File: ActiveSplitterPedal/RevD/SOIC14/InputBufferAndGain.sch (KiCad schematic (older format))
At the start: 7 parts, among them U2 TL072

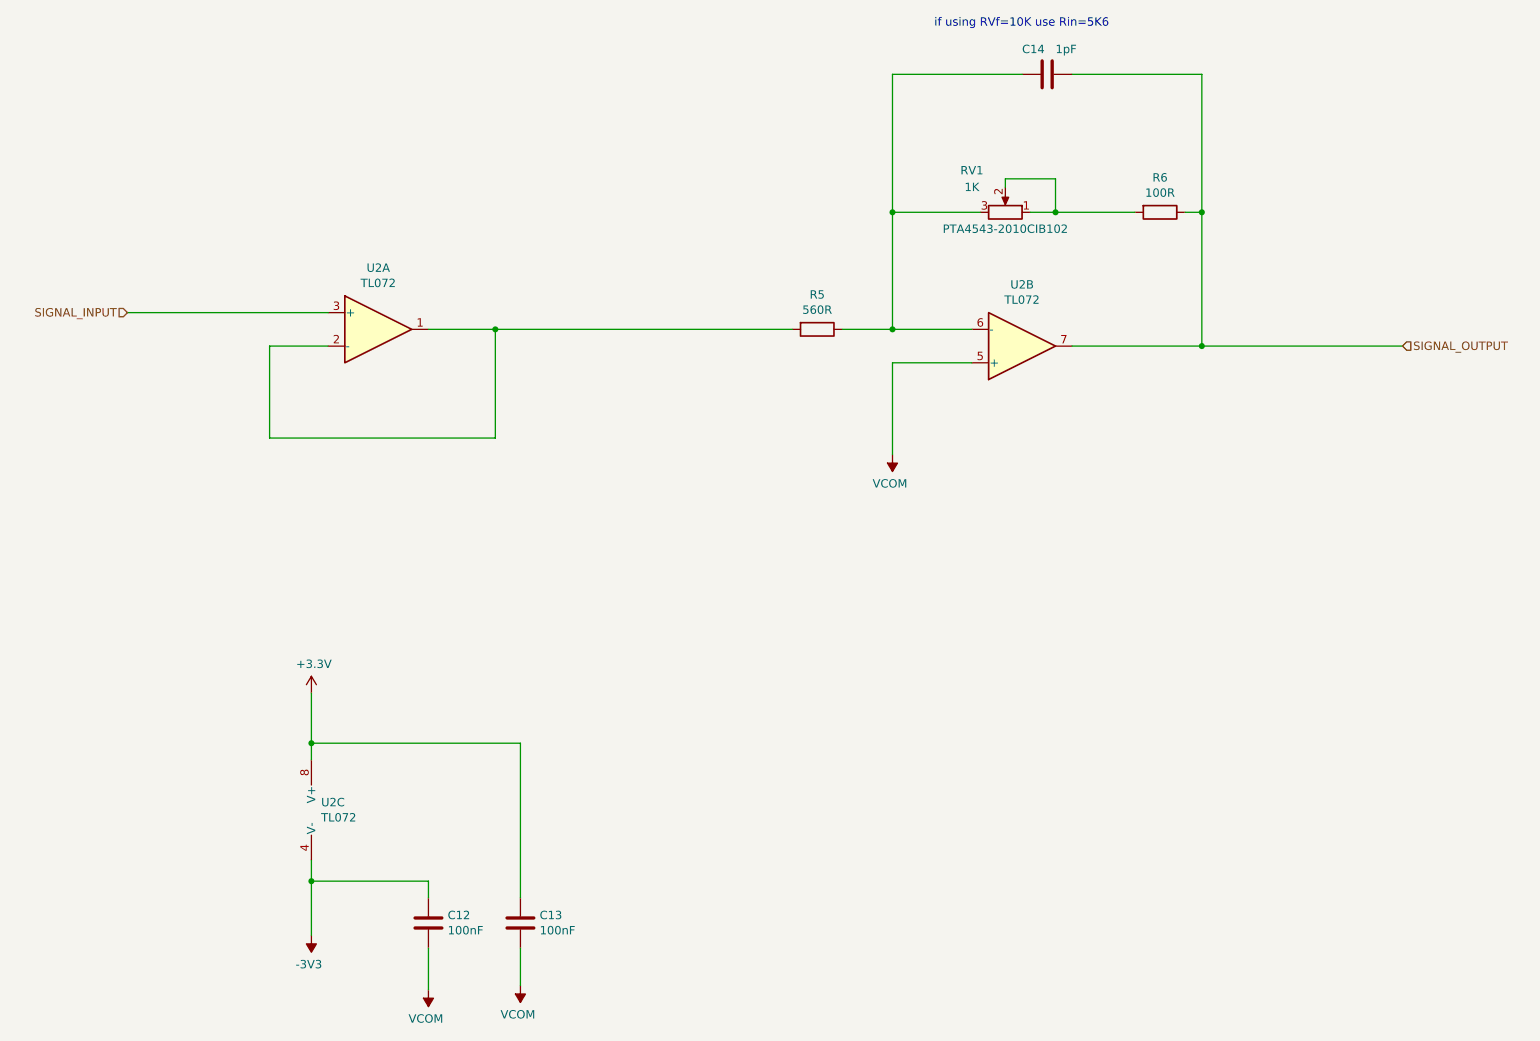
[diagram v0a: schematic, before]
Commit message: fixed peak detector
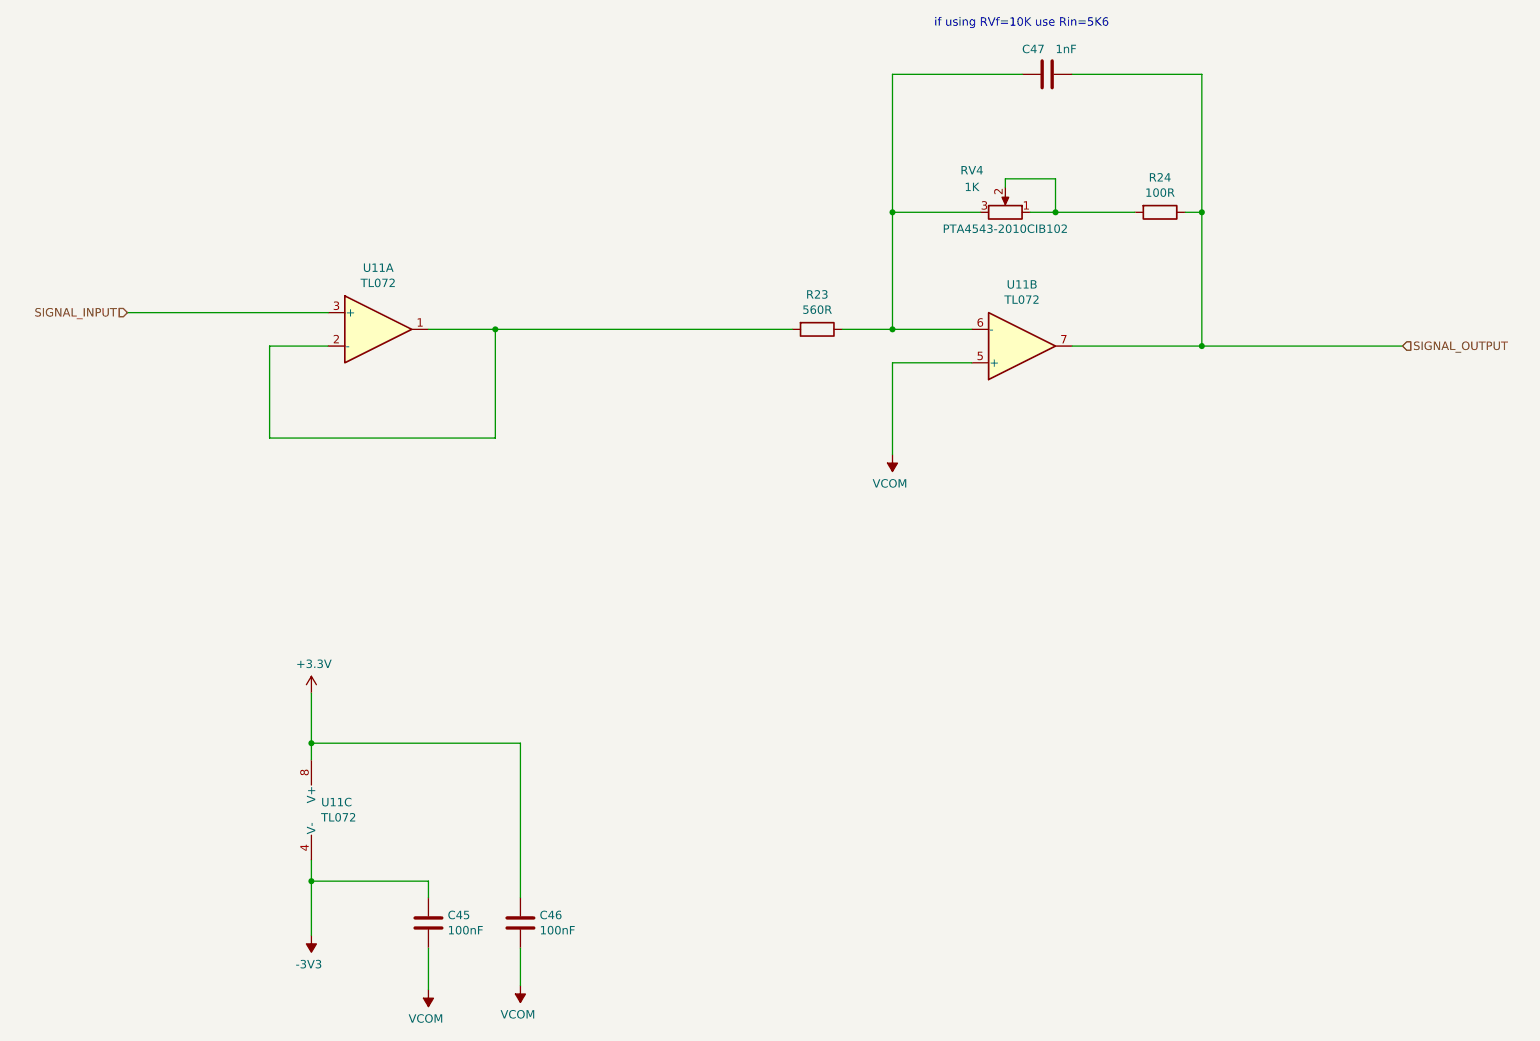
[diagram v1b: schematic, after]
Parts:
- C14: value 1pF -> 1nF
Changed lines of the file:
@@
 AR Path="/5F6A445C/5F59292E" Ref="R17"  Part="1"
 AR Path="/5F6AEF24/5F59292E" Ref="R23"  Part="1"
-F 0 "R5" V 6018 2875 50  0000 C CNN
+F 0 "R23" V 6018 2875 50  0000 C CNN
 F 1 "560R" V 6109 2875 50  0000 C CNN
 F 2 "Resistor_SMD:R_0805_2012Metric_Pad1.15x1.40mm_HandSolder" V 6155 2875 50  0001 C CNN
@@
 AR Path="/5F6A445C/5F59293F" Ref="RV3"  Part="1"
 AR Path="/5F6AEF24/5F59293F" Ref="RV4"  Part="1"
-F 0 "RV1" V 7600 1975 50  0000 C CNN
+F 0 "RV4" V 7600 1975 50  0000 C CNN
 F 1 "1K" V 7500 1975 50  0000 C CNN
 F 2 "Bourn_PTA_Slider:Slider_PTA4543_60MM" H 7350 2175 50  0001 C CNN
@@
 AR Path="/5F6A445C/5F592956" Ref="R18"  Part="1"
 AR Path="/5F6AEF24/5F592956" Ref="R24"  Part="1"
-F 0 "R6" V 8068 2175 50  0000 C CNN
+F 0 "R24" V 8068 2175 50  0000 C CNN
 F 1 "100R" V 8159 2175 50  0000 C CNN
 F 2 "Resistor_SMD:R_0805_2012Metric_Pad1.15x1.40mm_HandSolder" V 8205 2175 50  0001 C CNN
@@
 AR Path="/5F6A445C/5F59295D" Ref="C36"  Part="1"
 AR Path="/5F6AEF24/5F59295D" Ref="C47"  Part="1"
-F 0 "C14" V 7450 1200 50  0000 L CNN
-F 1 "1pF" V 7450 1400 50  0000 L CNN
+F 0 "C47" V 7450 1200 50  0000 L CNN
+F 1 "1nF" V 7450 1400 50  0000 L CNN
 F 2 "Capacitor_SMD:C_0805_2012Metric_Pad1.15x1.40mm_HandSolder" H 7638 1200 50  0001 C CNN
 F 3 "~" H 7600 1350 50  0001 C CNN
@@
 AR Path="/5F6A445C/5F59AE7C" Ref="U8"  Part="1"
 AR Path="/5F6AEF24/5F59AE7C" Ref="U11"  Part="1"
-F 0 "U2" H 3600 3242 50  0000 C CNN
+F 0 "U11" H 3600 3242 50  0000 C CNN
 F 1 "TL072" H 3600 3151 50  0000 C CNN
 F 2 "Package_SO:SOIC-8_3.9x4.9mm_P1.27mm" H 3600 2875 50  0001 C CNN
@@
 AR Path="/5F6A445C/5F59C9C2" Ref="U8"  Part="2"
 AR Path="/5F6AEF24/5F59C9C2" Ref="U11"  Part="2"
-F 0 "U2" H 7450 2608 50  0000 C CNN
+F 0 "U11" H 7450 2608 50  0000 C CNN
 F 1 "TL072" H 7450 2699 50  0000 C CNN
 F 2 "Package_SO:SOIC-8_3.9x4.9mm_P1.27mm" H 7450 2975 50  0001 C CNN
@@
 AR Path="/5F6A445C/5F59E5A5" Ref="U8"  Part="3"
 AR Path="/5F6AEF24/5F59E5A5" Ref="U11"  Part="3"
-F 0 "U2" H 3258 5796 50  0000 L CNN
+F 0 "U11" H 3258 5796 50  0000 L CNN
 F 1 "TL072" H 3258 5705 50  0000 L CNN
 F 2 "Package_SO:SOIC-8_3.9x4.9mm_P1.27mm" H 3300 5750 50  0001 C CNN
@@
 AR Path="/5F6A445C/5F5D3555" Ref="C34"  Part="1"
 AR Path="/5F6AEF24/5F5D3555" Ref="C45"  Part="1"
-F 0 "C12" H 4015 6471 50  0000 L CNN
+F 0 "C45" H 4015 6471 50  0000 L CNN
 F 1 "100nF" H 4015 6380 50  0000 L CNN
 F 2 "Capacitor_SMD:C_0805_2012Metric_Pad1.15x1.40mm_HandSolder" H 3938 6275 50  0001 C CNN
@@
 AR Path="/5F6A445C/5F5D446F" Ref="C35"  Part="1"
 AR Path="/5F6AEF24/5F5D446F" Ref="C46"  Part="1"
-F 0 "C13" H 4565 6471 50  0000 L CNN
+F 0 "C46" H 4565 6471 50  0000 L CNN
 F 1 "100nF" H 4565 6380 50  0000 L CNN
 F 2 "Capacitor_SMD:C_0805_2012Metric_Pad1.15x1.40mm_HandSolder" H 4488 6275 50  0001 C CNN
@@
 AR Path="/5F6A445C/5F594A1A" Ref="#PWR0135"  Part="1"
 AR Path="/5F6AEF24/5F594A1A" Ref="#PWR0147"  Part="1"
-F 0 "#PWR0111" H 3900 6675 50  0001 C CNN
+F 0 "#PWR0147" H 3900 6675 50  0001 C CNN
 F 1 "VCOM" H 3915 6998 50  0000 C CNN
 F 2 "" H 3900 6825 50  0001 C CNN
@@
 AR Path="/5F6A445C/5F59500E" Ref="#PWR0136"  Part="1"
 AR Path="/5F6AEF24/5F59500E" Ref="#PWR0148"  Part="1"
-F 0 "#PWR0112" H 4450 6650 50  0001 C CNN
+F 0 "#PWR0148" H 4450 6650 50  0001 C CNN
 F 1 "VCOM" H 4465 6973 50  0000 C CNN
 F 2 "" H 4450 6800 50  0001 C CNN
@@
 AR Path="/5F6A445C/5F595416" Ref="#PWR0137"  Part="1"
 AR Path="/5F6AEF24/5F595416" Ref="#PWR0149"  Part="1"
-F 0 "#PWR0113" H 6675 3475 50  0001 C CNN
+F 0 "#PWR0149" H 6675 3475 50  0001 C CNN
 F 1 "VCOM" H 6690 3798 50  0000 C CNN
 F 2 "" H 6675 3625 50  0001 C CNN
@@
 AR Path="/5F6A445C/5F595ABA" Ref="#PWR0138"  Part="1"
 AR Path="/5F6AEF24/5F595ABA" Ref="#PWR0150"  Part="1"
-F 0 "#PWR0114" H 3200 6600 50  0001 C CNN
+F 0 "#PWR0150" H 3200 6600 50  0001 C CNN
 F 1 "-3V3" H 3215 6673 50  0000 C CNN
 F 2 "" H 3200 6500 50  0001 C CNN
@@
 AR Path="/5F6A445C/5F596316" Ref="#PWR0139"  Part="1"
 AR Path="/5F6AEF24/5F596316" Ref="#PWR0151"  Part="1"
-F 0 "#PWR0115" H 3200 4900 50  0001 C CNN
+F 0 "#PWR0151" H 3200 4900 50  0001 C CNN
 F 1 "+3.3V" H 3215 5223 50  0000 C CNN
 F 2 "" H 3200 5050 50  0001 C CNN

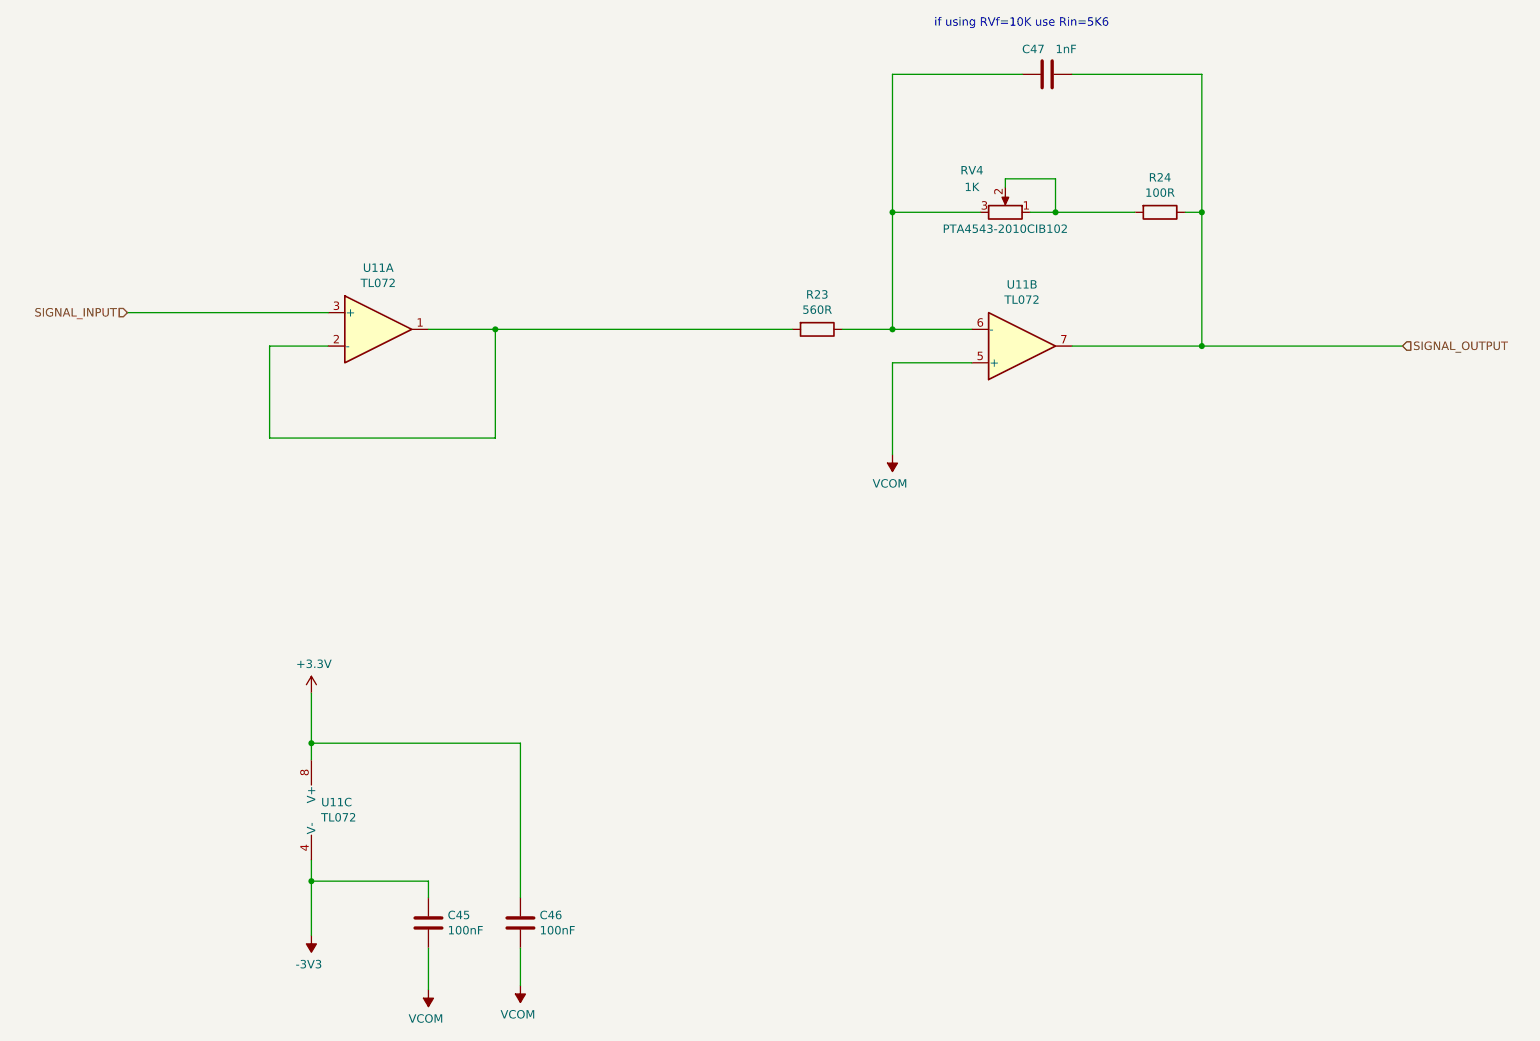
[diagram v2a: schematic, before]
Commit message: updated hw
- Changed peak detector gain feedback resistor to 10K
- Changed peak detector storage cap to 100nF
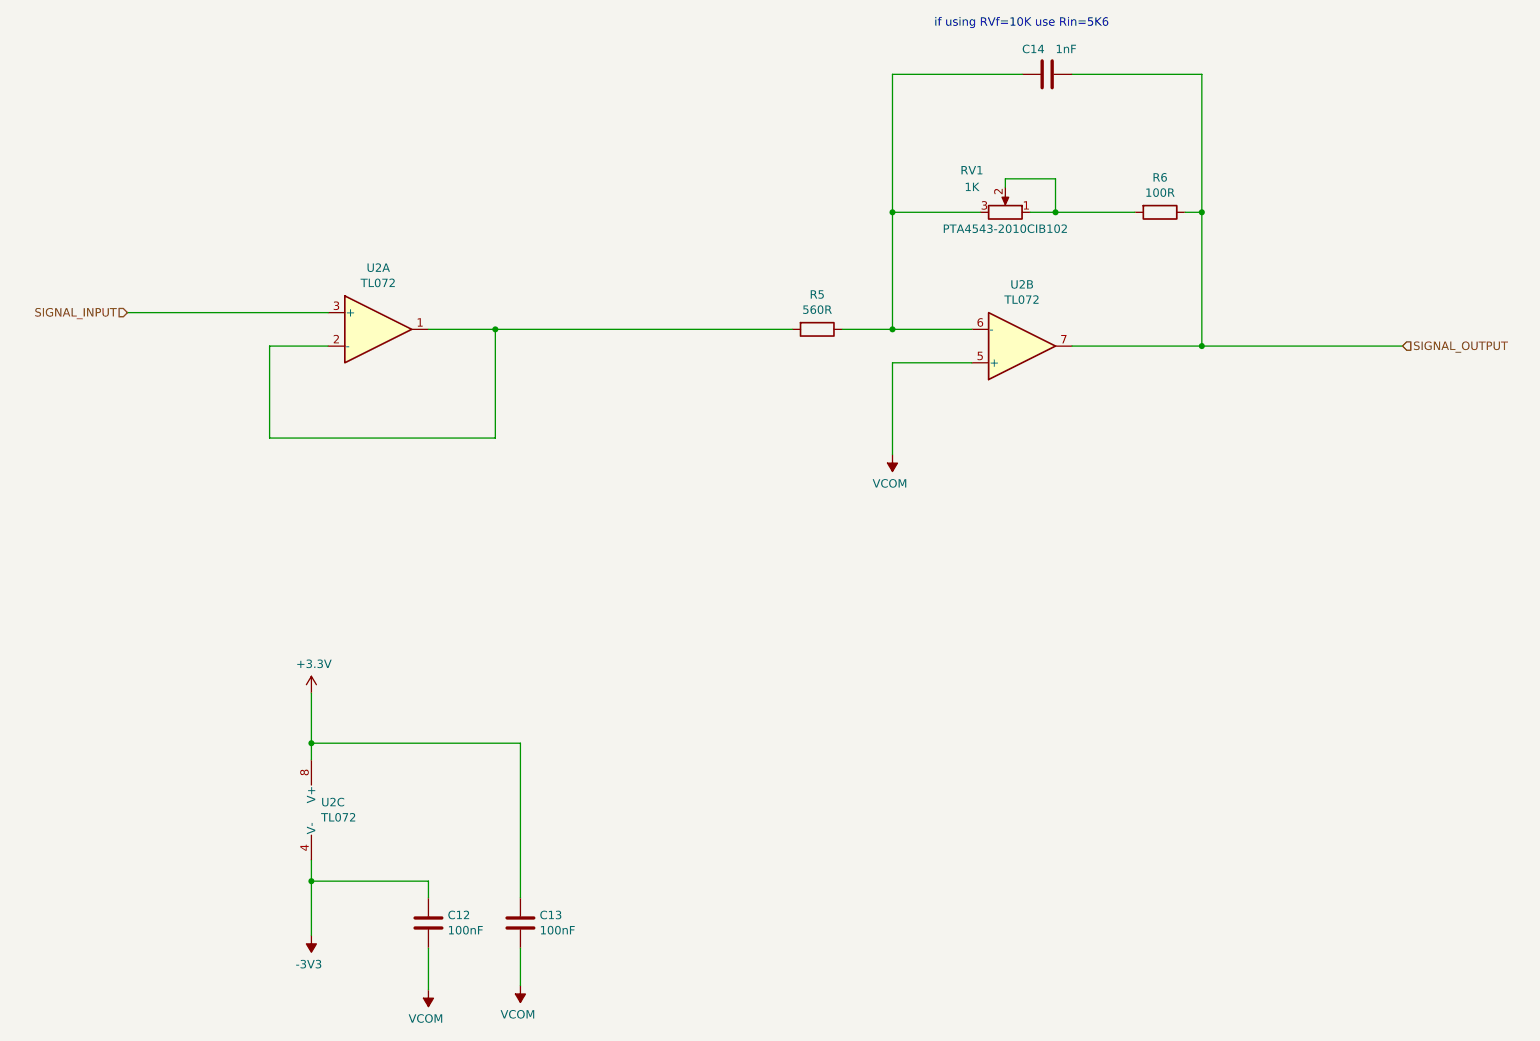
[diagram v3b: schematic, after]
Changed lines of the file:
@@
 $Descr A4 11693 8268
 encoding utf-8
-Sheet 10 10
+Sheet 4 10
 Title ""
 Date ""
@@
 AR Path="/5F6A445C/5F59292E" Ref="R17"  Part="1"
 AR Path="/5F6AEF24/5F59292E" Ref="R23"  Part="1"
-F 0 "R23" V 6018 2875 50  0000 C CNN
+F 0 "R5" V 6018 2875 50  0000 C CNN
 F 1 "560R" V 6109 2875 50  0000 C CNN
 F 2 "Resistor_SMD:R_0805_2012Metric_Pad1.15x1.40mm_HandSolder" V 6155 2875 50  0001 C CNN
@@
 AR Path="/5F6A445C/5F59293F" Ref="RV3"  Part="1"
 AR Path="/5F6AEF24/5F59293F" Ref="RV4"  Part="1"
-F 0 "RV4" V 7600 1975 50  0000 C CNN
+F 0 "RV1" V 7600 1975 50  0000 C CNN
 F 1 "1K" V 7500 1975 50  0000 C CNN
 F 2 "Bourn_PTA_Slider:Slider_PTA4543_60MM" H 7350 2175 50  0001 C CNN
@@
 AR Path="/5F6A445C/5F592956" Ref="R18"  Part="1"
 AR Path="/5F6AEF24/5F592956" Ref="R24"  Part="1"
-F 0 "R24" V 8068 2175 50  0000 C CNN
+F 0 "R6" V 8068 2175 50  0000 C CNN
 F 1 "100R" V 8159 2175 50  0000 C CNN
 F 2 "Resistor_SMD:R_0805_2012Metric_Pad1.15x1.40mm_HandSolder" V 8205 2175 50  0001 C CNN
@@
 AR Path="/5F6A445C/5F59295D" Ref="C36"  Part="1"
 AR Path="/5F6AEF24/5F59295D" Ref="C47"  Part="1"
-F 0 "C47" V 7450 1200 50  0000 L CNN
+F 0 "C14" V 7450 1200 50  0000 L CNN
 F 1 "1nF" V 7450 1400 50  0000 L CNN
 F 2 "Capacitor_SMD:C_0805_2012Metric_Pad1.15x1.40mm_HandSolder" H 7638 1200 50  0001 C CNN
@@
 AR Path="/5F6A445C/5F59AE7C" Ref="U8"  Part="1"
 AR Path="/5F6AEF24/5F59AE7C" Ref="U11"  Part="1"
-F 0 "U11" H 3600 3242 50  0000 C CNN
+F 0 "U2" H 3600 3242 50  0000 C CNN
 F 1 "TL072" H 3600 3151 50  0000 C CNN
 F 2 "Package_SO:SOIC-8_3.9x4.9mm_P1.27mm" H 3600 2875 50  0001 C CNN
@@
 AR Path="/5F6A445C/5F59C9C2" Ref="U8"  Part="2"
 AR Path="/5F6AEF24/5F59C9C2" Ref="U11"  Part="2"
-F 0 "U11" H 7450 2608 50  0000 C CNN
+F 0 "U2" H 7450 2608 50  0000 C CNN
 F 1 "TL072" H 7450 2699 50  0000 C CNN
 F 2 "Package_SO:SOIC-8_3.9x4.9mm_P1.27mm" H 7450 2975 50  0001 C CNN
@@
 AR Path="/5F6A445C/5F59E5A5" Ref="U8"  Part="3"
 AR Path="/5F6AEF24/5F59E5A5" Ref="U11"  Part="3"
-F 0 "U11" H 3258 5796 50  0000 L CNN
+F 0 "U2" H 3258 5796 50  0000 L CNN
 F 1 "TL072" H 3258 5705 50  0000 L CNN
 F 2 "Package_SO:SOIC-8_3.9x4.9mm_P1.27mm" H 3300 5750 50  0001 C CNN
@@
 AR Path="/5F6A445C/5F5D3555" Ref="C34"  Part="1"
 AR Path="/5F6AEF24/5F5D3555" Ref="C45"  Part="1"
-F 0 "C45" H 4015 6471 50  0000 L CNN
+F 0 "C12" H 4015 6471 50  0000 L CNN
 F 1 "100nF" H 4015 6380 50  0000 L CNN
 F 2 "Capacitor_SMD:C_0805_2012Metric_Pad1.15x1.40mm_HandSolder" H 3938 6275 50  0001 C CNN
@@
 AR Path="/5F6A445C/5F5D446F" Ref="C35"  Part="1"
 AR Path="/5F6AEF24/5F5D446F" Ref="C46"  Part="1"
-F 0 "C46" H 4565 6471 50  0000 L CNN
+F 0 "C13" H 4565 6471 50  0000 L CNN
 F 1 "100nF" H 4565 6380 50  0000 L CNN
 F 2 "Capacitor_SMD:C_0805_2012Metric_Pad1.15x1.40mm_HandSolder" H 4488 6275 50  0001 C CNN
@@
 AR Path="/5F6A445C/5F594A1A" Ref="#PWR0135"  Part="1"
 AR Path="/5F6AEF24/5F594A1A" Ref="#PWR0147"  Part="1"
-F 0 "#PWR0147" H 3900 6675 50  0001 C CNN
+F 0 "#PWR0111" H 3900 6675 50  0001 C CNN
 F 1 "VCOM" H 3915 6998 50  0000 C CNN
 F 2 "" H 3900 6825 50  0001 C CNN
@@
 AR Path="/5F6A445C/5F59500E" Ref="#PWR0136"  Part="1"
 AR Path="/5F6AEF24/5F59500E" Ref="#PWR0148"  Part="1"
-F 0 "#PWR0148" H 4450 6650 50  0001 C CNN
+F 0 "#PWR0112" H 4450 6650 50  0001 C CNN
 F 1 "VCOM" H 4465 6973 50  0000 C CNN
 F 2 "" H 4450 6800 50  0001 C CNN
@@
 AR Path="/5F6A445C/5F595416" Ref="#PWR0137"  Part="1"
 AR Path="/5F6AEF24/5F595416" Ref="#PWR0149"  Part="1"
-F 0 "#PWR0149" H 6675 3475 50  0001 C CNN
+F 0 "#PWR0113" H 6675 3475 50  0001 C CNN
 F 1 "VCOM" H 6690 3798 50  0000 C CNN
 F 2 "" H 6675 3625 50  0001 C CNN
@@
 AR Path="/5F6A445C/5F595ABA" Ref="#PWR0138"  Part="1"
 AR Path="/5F6AEF24/5F595ABA" Ref="#PWR0150"  Part="1"
-F 0 "#PWR0150" H 3200 6600 50  0001 C CNN
+F 0 "#PWR0114" H 3200 6600 50  0001 C CNN
 F 1 "-3V3" H 3215 6673 50  0000 C CNN
 F 2 "" H 3200 6500 50  0001 C CNN
@@
 AR Path="/5F6A445C/5F596316" Ref="#PWR0139"  Part="1"
 AR Path="/5F6AEF24/5F596316" Ref="#PWR0151"  Part="1"
-F 0 "#PWR0151" H 3200 4900 50  0001 C CNN
+F 0 "#PWR0115" H 3200 4900 50  0001 C CNN
 F 1 "+3.3V" H 3215 5223 50  0000 C CNN
 F 2 "" H 3200 5050 50  0001 C CNN
